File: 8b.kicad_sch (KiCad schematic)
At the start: 61 parts, among them J1 AudioJack2, J11 AudioJack3, J2 AudioJack2, J3 AudioJack2, J4 AudioJack2, J5 AudioJack2, J6 AudioJack2, J7 AudioJack2, J8 AudioJack2, J9 AudioJack3, Q1 2N3904, Q2 2N3904, Q3 2N3904, Q4 2N3904, Q5 2N3904, Q6 2N3904, Q7 2N3904, Q8 2N3904, SW1 SW_Push, SW2 SW_Push, SW3 SW_Push, SW4 SW_Push, SW5 SW_Push, SW6 SW_Push, SW7 SW_Push, SW8 SW_Push, SW9 SW_Push_DPDT, U1 Pico

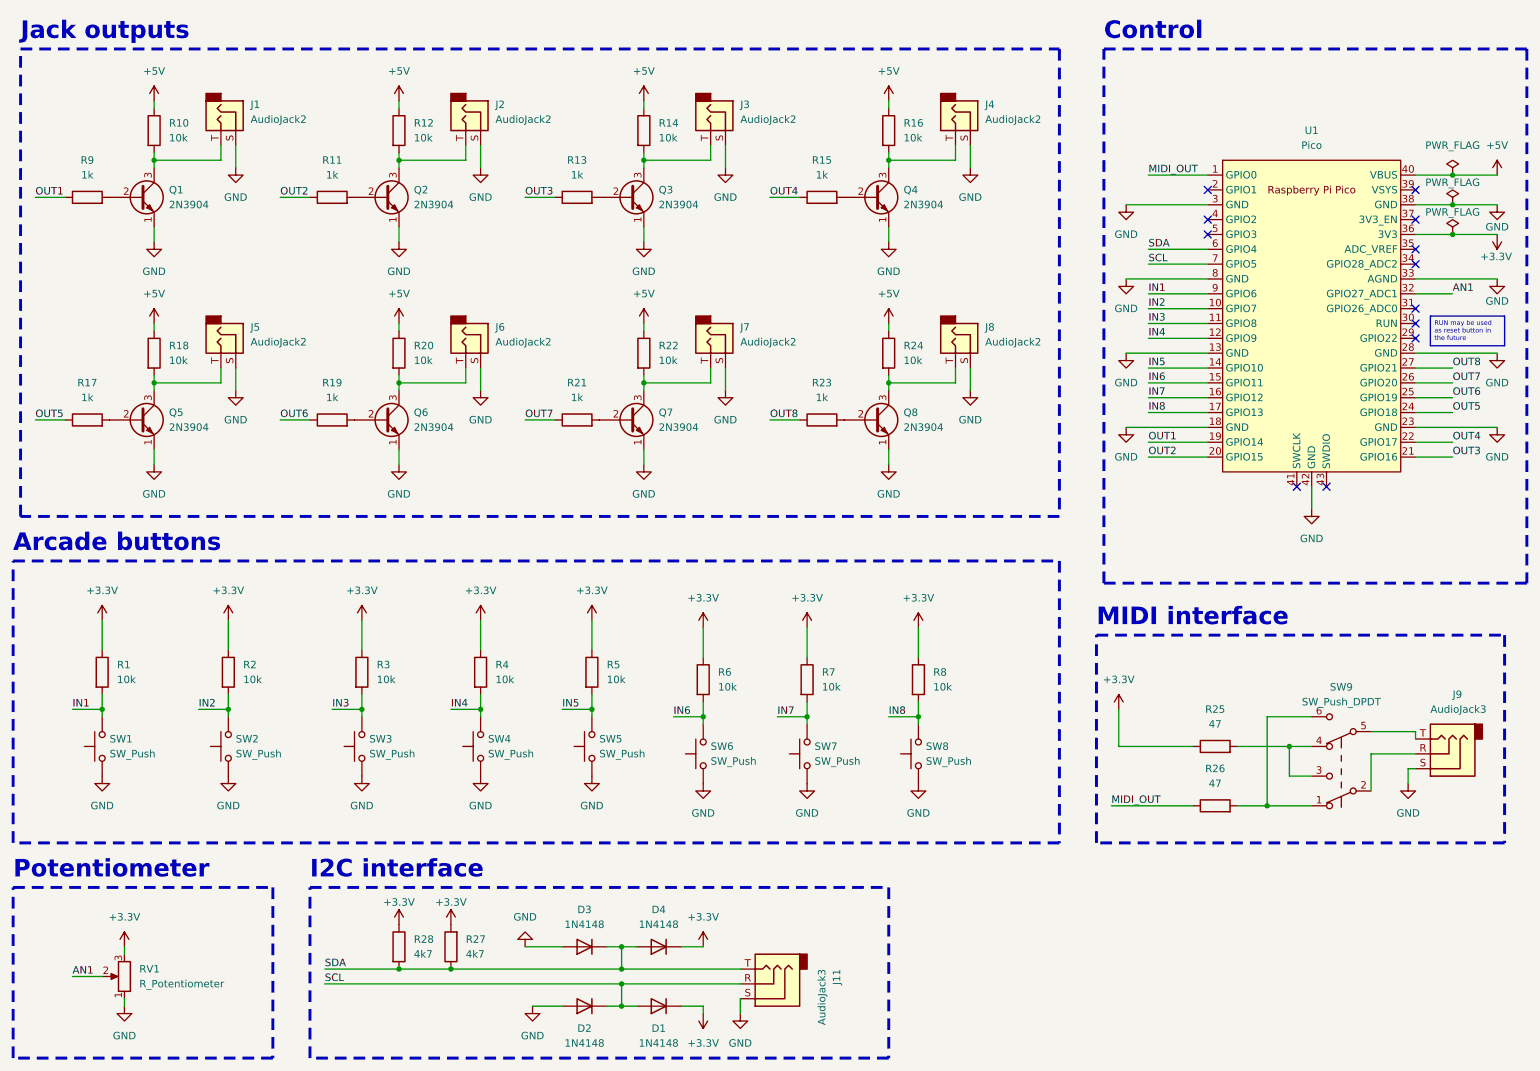
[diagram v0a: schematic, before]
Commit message: Update some footprints
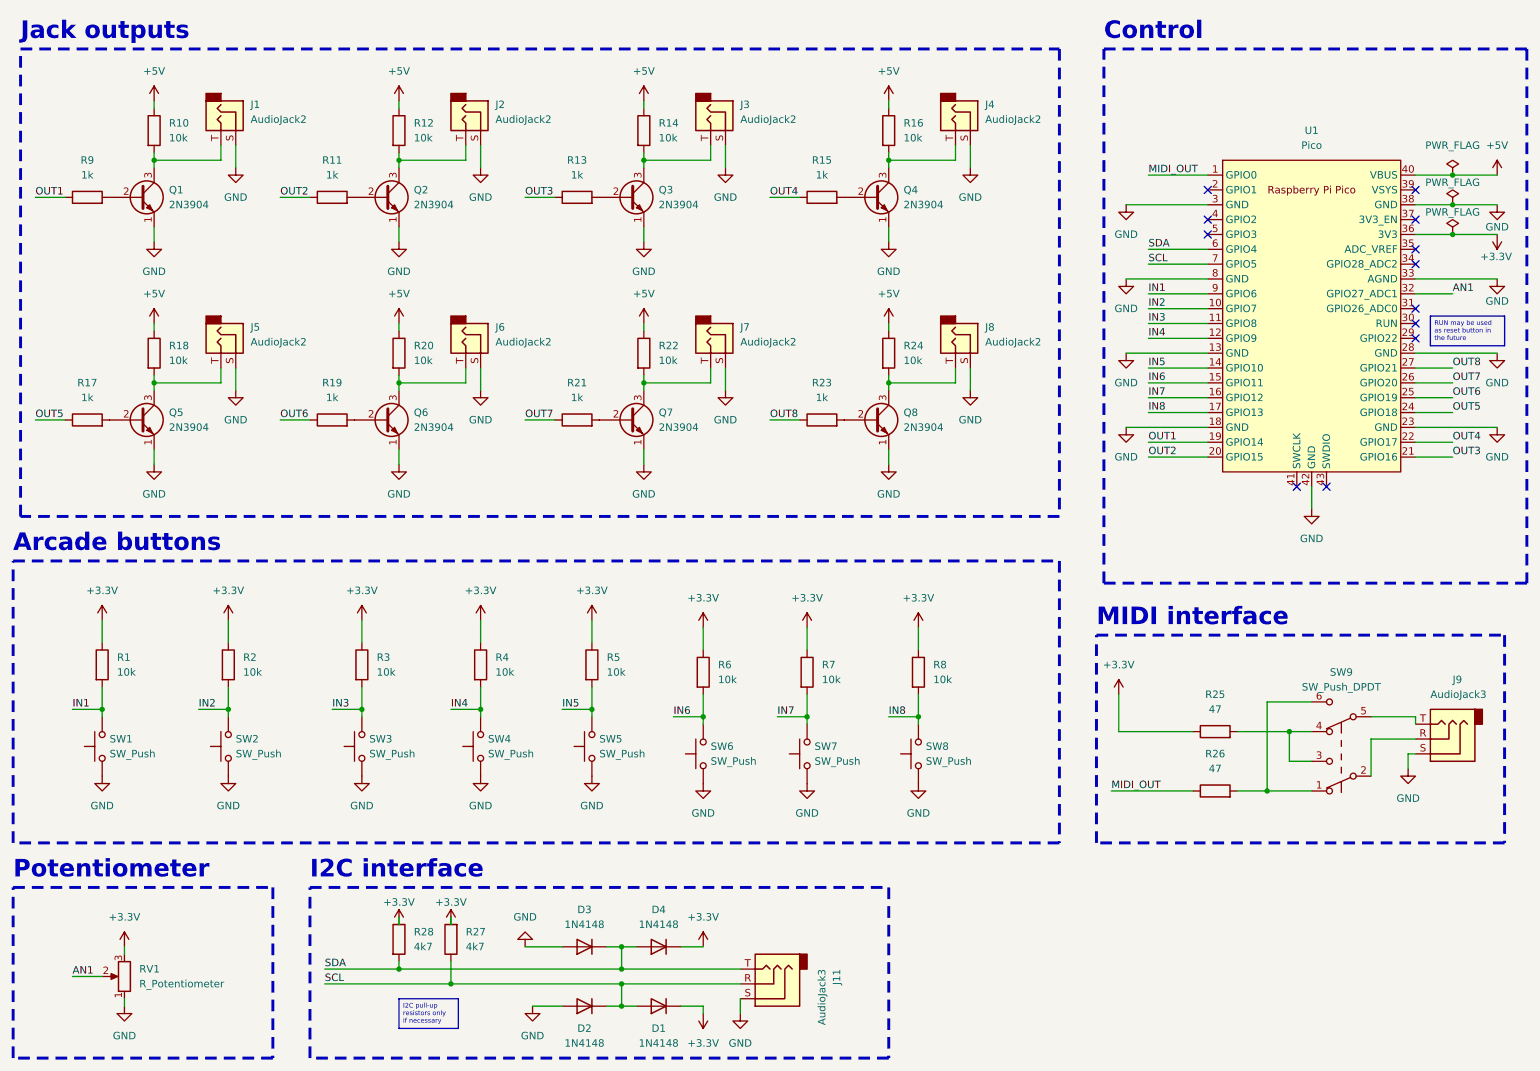
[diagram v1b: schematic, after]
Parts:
- J1, J11, J2, J3, J4, J5, J6, J7, J8, J9: footprint (none) -> AudioJacks:Jack_3.5mm_QingPu_WQP-PJ302M_Horizontal
- R1, R10, R11, R12, R13, R14, R15, R16, R17, R18, R19, R2, R20, R21, R22, R23, R24, R25, R26, R27, R28, R3, R4, R5, R6, R7, R8, R9: footprint (none) -> Resistor_THT:R_Axial_DIN0207_L6.3mm_D2.5mm_P10.16mm_Horizontal
- RV1: footprint (none) -> Potentiometer_THT:Potentiometer_Bourns_PTV09A-1_Single_Vertical
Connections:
- net SCL: now also R27.1
- net SDA: no longer R27.1
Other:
- moved on the sheet: J9, R1, R2, R25, R26, R27, R28, R3, R4, R5, R6, R7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

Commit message: Add missing footprints
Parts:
- D1: footprint Diode_THT:D_DO-35_SOD27_P7.62mm_Horizontal -> ArcadeButtons:sanwa-obsf-30-g
- RV1: footprint Potentiometer_THT:Potentiometer_Bourns_PTV09A-1_Single_Vertical -> Potentiometer_THT_mod:Potentiometer_Bourns_PTV09A-1_Single_Vertical
- SW1, SW2, SW3, SW4, SW5, SW6, SW7, SW8: footprint (none) -> ArcadeButtons:sanwa-obsf-30-g
- SW9: footprint (none) -> SparkFun-Electromechanical:EG2211
- U1: footprint RPi_Pico:RPi_Pico_SMD_TH -> RPi Pico:RPi_Pico_SMD_TH
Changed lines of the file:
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@@
       (effects (font (size 1.27 1.27)) (justify right))
     )
-    (property "Footprint" "" (at 52.07 140.97 0)
+    (property "Footprint" "ArcadeButtons:sanwa-obsf-30-g" (at 52.07 140.97 0)
       (effects (font (size 1.27 1.27)) hide)
     )
@@
       (effects (font (size 1.27 1.27)) (justify right))
     )
-    (property "Footprint" "" (at 30.48 140.97 0)
+    (property "Footprint" "ArcadeButtons:sanwa-obsf-30-g" (at 30.48 140.97 0)
       (effects (font (size 1.27 1.27)) hide)
     )
@@
       (effects (font (size 1.27 1.27)) (justify right))
     )
-    (property "Footprint" "Potentiometer_THT:Potentiometer_Bourns_PTV09A-1_Single_Vertical" (at 39.37 180.34 0)
+    (property "Footprint" "Potentiometer_THT_mod:Potentiometer_Bourns_PTV09A-1_Single_Vertical" (at 39.37 180.34 0)
       (effects (font (size 1.27 1.27)) hide)
     )
@@
       (effects (font (size 1.27 1.27)) (justify right))
     )
-    (property "Footprint" "" (at 151.13 142.24 0)
+    (property "Footprint" "ArcadeButtons:sanwa-obsf-30-g" (at 151.13 142.24 0)
       (effects (font (size 1.27 1.27)) hide)
     )
@@
       (effects (font (size 1.27 1.27)) (justify right))
     )
-    (property "Footprint" "" (at 95.25 140.97 0)
+    (property "Footprint" "ArcadeButtons:sanwa-obsf-30-g" (at 95.25 140.97 0)
       (effects (font (size 1.27 1.27)) hide)
     )
@@
       (effects (font (size 1.27 1.27)) (justify right))
     )
-    (property "Footprint" "" (at 170.18 142.24 0)
+    (property "Footprint" "ArcadeButtons:sanwa-obsf-30-g" (at 170.18 142.24 0)
       (effects (font (size 1.27 1.27)) hide)
     )
@@
       (effects (font (size 1.27 1.27)) (justify right))
     )
-    (property "Footprint" "" (at 133.35 142.24 0)
+    (property "Footprint" "ArcadeButtons:sanwa-obsf-30-g" (at 133.35 142.24 0)
       (effects (font (size 1.27 1.27)) hide)
     )
@@
       (effects (font (size 1.27 1.27)))
     )
-    (property "Footprint" "" (at 247.65 146.05 0)
+    (property "Footprint" "SparkFun-Electromechanical:EG2211" (at 247.65 146.05 0)
       (effects (font (size 1.27 1.27)) hide)
     )
@@
       (effects (font (size 1.27 1.27)) (justify right))
     )
-    (property "Footprint" "" (at 74.93 140.97 0)
+    (property "Footprint" "ArcadeButtons:sanwa-obsf-30-g" (at 74.93 140.97 0)
       (effects (font (size 1.27 1.27)) hide)
     )
@@
       (effects (font (size 1.27 1.27)) (justify right))
     )
-    (property "Footprint" "" (at 114.3 140.97 0)
+    (property "Footprint" "ArcadeButtons:sanwa-obsf-30-g" (at 114.3 140.97 0)
       (effects (font (size 1.27 1.27)) hide)
     )
@@
       (effects (font (size 1.27 1.27)))
     )
-    (property "Footprint" "RPi_Pico:RPi_Pico_SMD_TH" (at 242.57 67.31 90)
+    (property "Footprint" "RPi Pico:RPi_Pico_SMD_TH" (at 242.57 67.31 90)
       (effects (font (size 1.27 1.27)) hide)
     )
@@
       (effects (font (size 1.27 1.27)))
     )
-    (property "Footprint" "Diode_THT:D_DO-35_SOD27_P7.62mm_Horizontal" (at 130.81 185.42 0)
-      (effects (font (size 1.27 1.27)) hide)
-    )
+    (property "Footprint" "ArcadeButtons:sanwa-obsf-30-g" (at 130.81 185.42 0)
+      (effects (font (size 1.27 1.27)) hide)
+    )

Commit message: Update footprint components
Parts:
- D1: footprint ArcadeButtons:sanwa-obsf-30-g -> Diode_THT:D_DO-35_SOD27_P7.62mm_Horizontal
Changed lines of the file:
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@@
       (effects (font (size 1.27 1.27)))
     )
-    (property "Footprint" "ArcadeButtons:sanwa-obsf-30-g" (at 130.81 185.42 0)
+    (property "Footprint" "Diode_THT:D_DO-35_SOD27_P7.62mm_Horizontal" (at 130.81 185.42 0)
       (effects (font (size 1.27 1.27)) hide)
     )
